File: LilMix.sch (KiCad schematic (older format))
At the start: 0 parts

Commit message: Initial version of circuit
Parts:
- added C1, C2: 10uF, symbol Device:CP
- added C? (x4): 47pF, symbol 4ms-passives:C
- added C? (x4): 100pF, symbol 4ms-passives:C
- added D1, D2: 1N5819, symbol 4ms-passives:D_Schottky
- added J1_L, J1_R, J2_L, J2_R, J3_L, J3_R, J5, J6, J? (x2): PJ301BM, Eurocad:EighthInch_PJ301BM_CC_FIXED, symbol eurocad:PJ301M-12
- added JP1: EURO_HEADER_10pin, 4ms-footprints:Header_2x05_Pitch2.54mm_TH_-12v_Label, symbol 4ms-headers:EURO_HEADER_10pin
- added R? (x8): 10k, symbol 4ms-passives:R
- added R? (x6): 100k, symbol 4ms-passives:R
- added R? (x2): 330r, symbol 4ms-passives:R
- added R? (x2): 39k, symbol 4ms-passives:R
- added R? (x2): 75r, symbol 4ms-passives:R
- added RV? (x8): A100k, symbol 4ms-mech:POT_DUAL
- added U? (x5): TL074, symbol Amplifier_Operational:TL074
- added U? (x3): NE5532, symbol Amplifier_Operational:NE5532
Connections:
- net +12V: now also C1.1, C?.1, C?.1, D1.1 (K), U?.4 (V+), U?.8 (V+)
- net -12V: now also C2.2, C?.2, C?.2, D2.2 (A), U?.11 (V-), U?.4 (V-)
- new net: D2.1 (K), JP1.10 (-12V)
- new net: D1.2 (A), JP1.2 (+12V)
- new net: C?.2, R?.1, R?.2, U?.13 (-)
- new net: C?.2, R?.1, R?.1, R?.1, R?.2, U?.2 (-)
- new net: R?.2, RV?.2 (Center) (x4)
- new net: J1_R.3, RV?.6 (Right)
- new net: J2_R.3, RV?.6 (Right)
- new net: J3_R.3, RV?.6 (Right)
- new net: C?.2, R?.1, R?.1, R?.1, R?.2, U?.6 (-)
- new net: R?.2, RV?.5 (Center) (x4)
- new net: J5.3, R?.1
- new net: J6.3, R?.1
- new net: C?.1, R?.1, R?.2, U?.8
- new net: C?.1, R?.1, R?.2, U?.14
- new net: C?.2, R?.1, R?.2, U?.9 (-)
- new net: R?.1, R?.2, U?.1
- new net: R?.1, R?.2, U?.2 (-)
- new net: R?.1, R?.2, U?.6 (-)
- new net: R?.1, R?.2, U?.7
- new net: J?.3, R?.1 (x2)
- new net GND: C1.2, C2.1, C?.1, C?.1, C?.2, C?.2, J1_L.1, J1_R.1, J2_L.1, J2_R.1, J3_L.1, J3_R.1, J5.1, J6.1, J?.1, J?.1, JP1.3 (GND), JP1.4 (GND), JP1.5 (GND), JP1.6 (GND), JP1.7 (GND), JP1.8 (GND), RV?.1 (Left), RV?.1 (Left), RV?.1 (Left), RV?.1 (Left), RV?.4 (Left), RV?.4 (Left), RV?.4 (Left), RV?.4 (Left), U?.10 (+), U?.12 (+), U?.3 (+), U?.3 (+), U?.5 (+), U?.5 (+)
- new net J1_INSERT: J1_L.3, J1_R.2, J3_R.2, RV?.3 (Right)
- new net J2_INSERT: J2_L.3, J2_R.2, RV?.3 (Right)
- new net J3_INSERT: J3_L.3, RV?.3 (Right)
- new net L_INV: C?.1, R?.1, R?.2, RV?.3 (Right), U?.1
- new net R_INV: C?.1, R?.1, R?.2, RV?.6 (Right), U?.7
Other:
- note added: "LilMix"

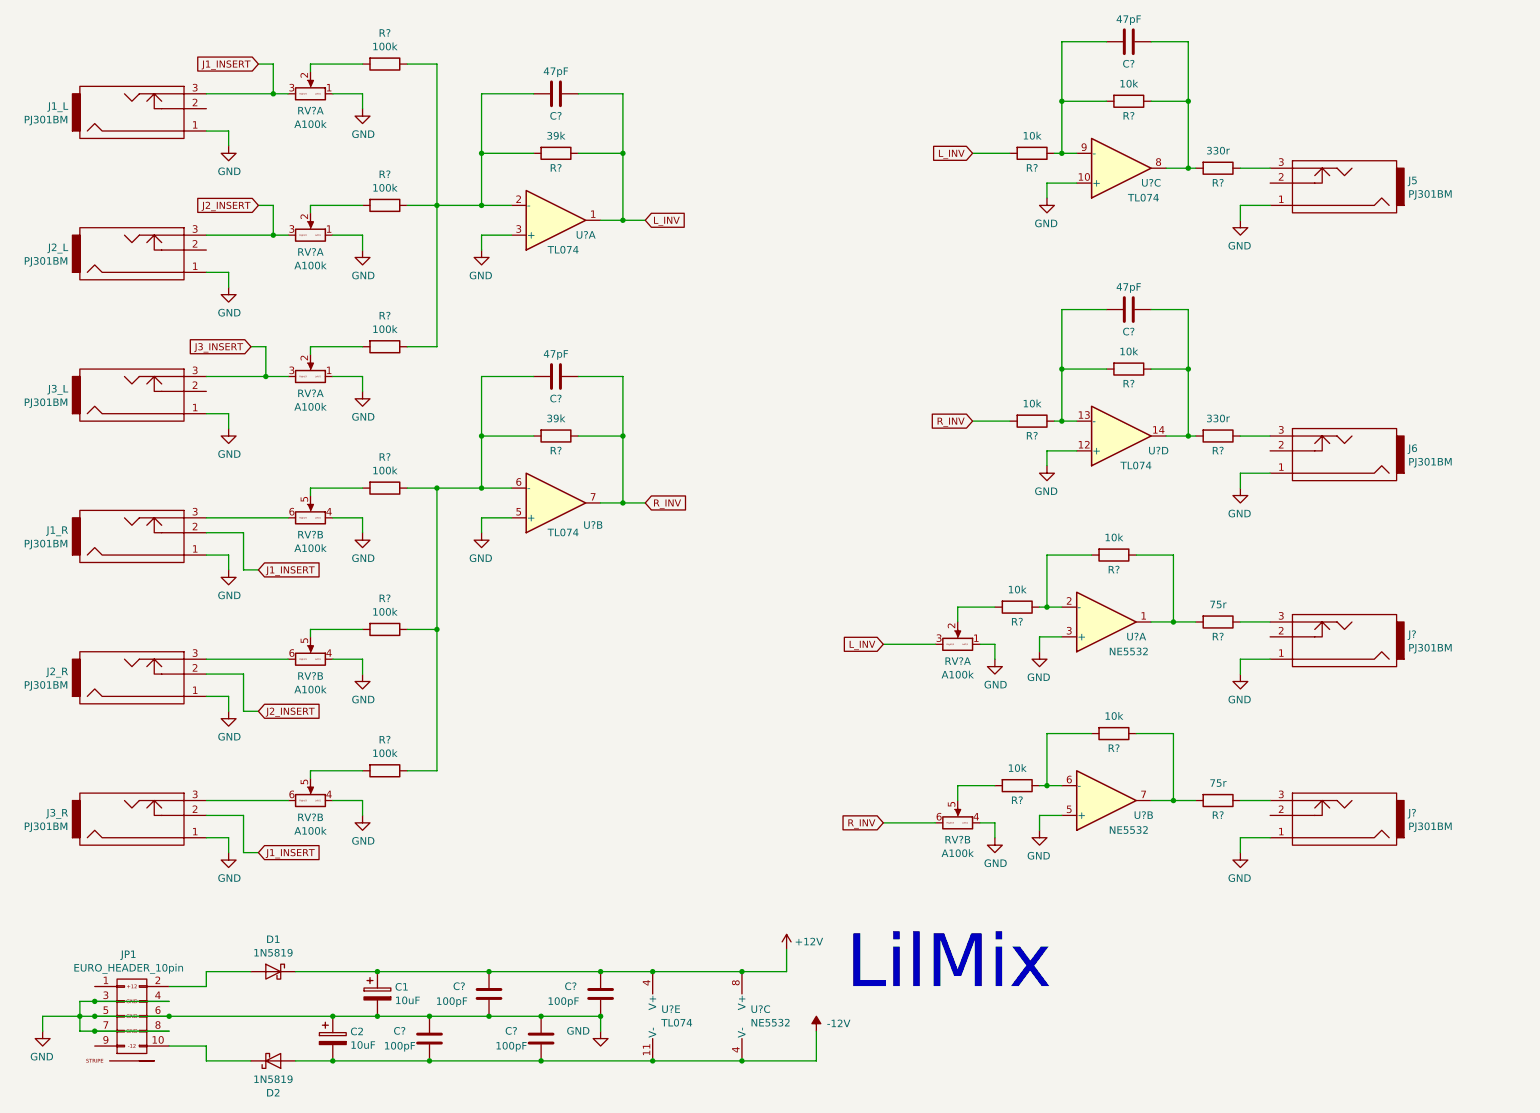
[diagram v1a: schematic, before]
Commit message: Updated to stereo jacks, replaced IC caps
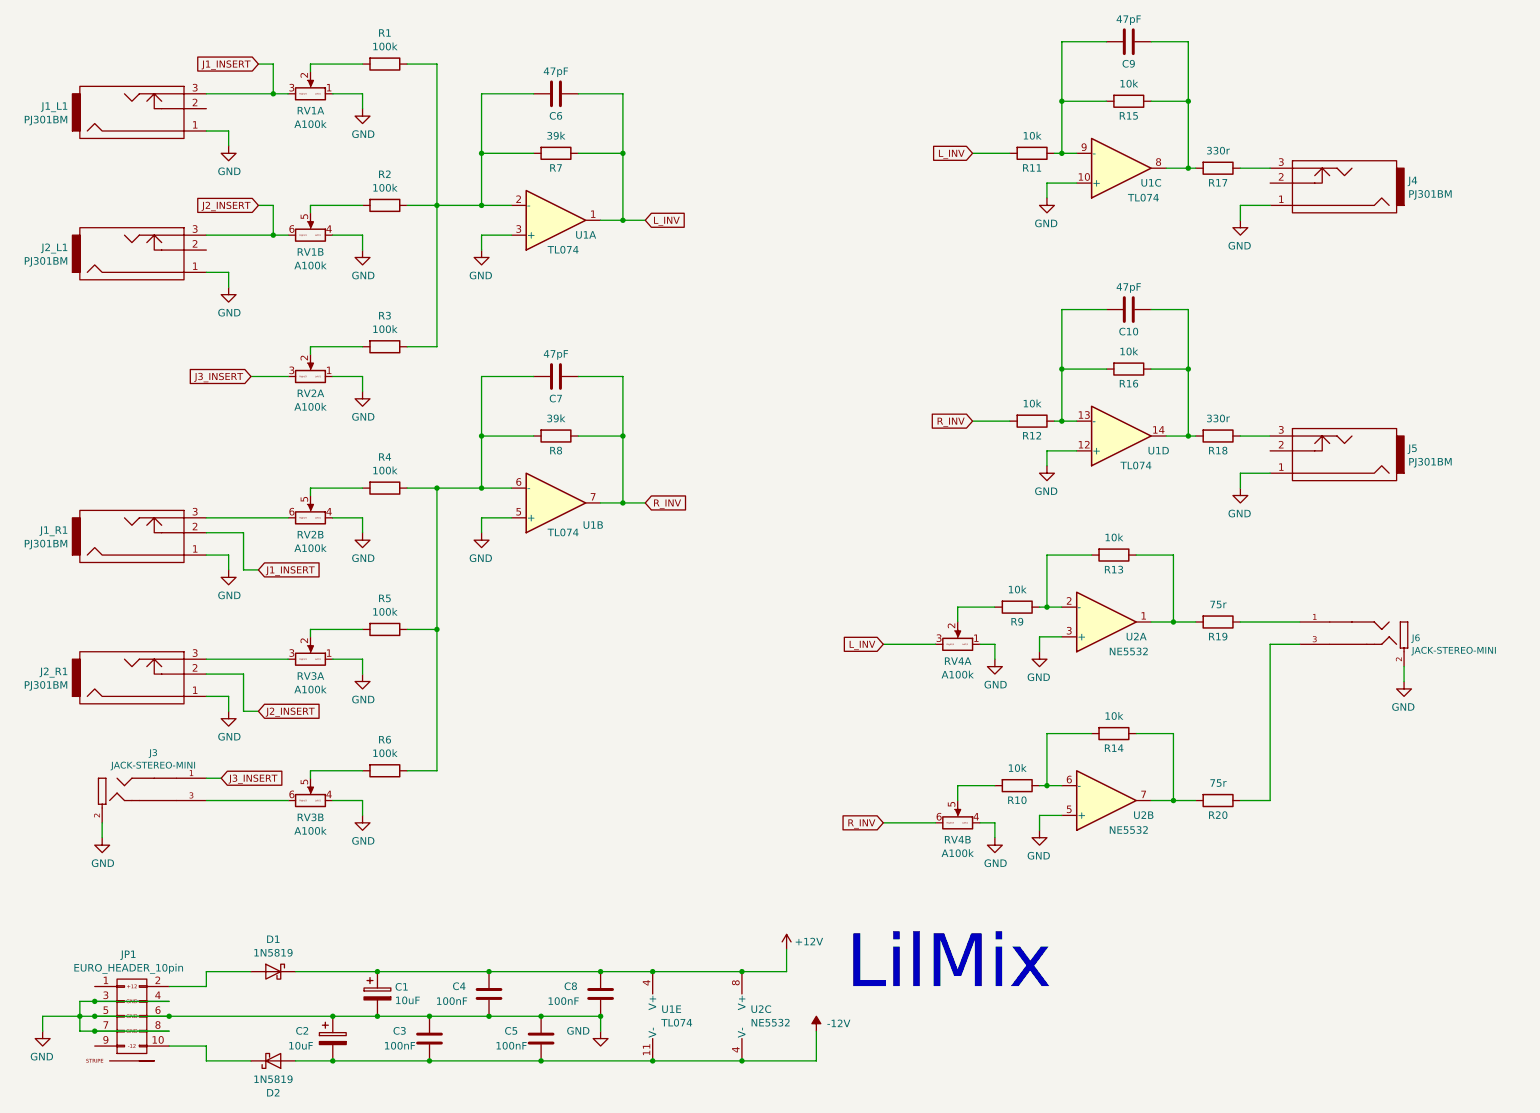
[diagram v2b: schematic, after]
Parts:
- removed J3_L, J3_R, J? (x2): PJ301BM, Eurocad:EighthInch_PJ301BM_CC_FIXED, symbol eurocad:PJ301M-12
- added J3, J6: JACK-STEREO-MINI, 4ms-footprints:PJ301M-12, symbol 4ms-mech:JACK-STEREO-MINI
- C1, C2: footprint (none) -> Capacitor_SMD:C_0805_2012Metric_Pad1.15x1.40mm_HandSolder
- C10, C6, C7, C9: renamed from C?; footprint (none) -> Capacitor_SMD:C_0805_2012Metric_Pad1.15x1.40mm_HandSolder
- C3, C4, C5, C8: renamed from C?; value 100pF -> 100nF; footprint (none) -> Capacitor_SMD:C_0805_2012Metric_Pad1.15x1.40mm_HandSolder
- D1, D2: footprint (none) -> Diode_SMD:D_SOD-123
- J1_L1: renamed from J1_L; footprint Eurocad:EighthInch_PJ301BM_CC_FIXED -> 4ms-footprints:PJ301M-12
- J1_R1: renamed from J1_R; footprint Eurocad:EighthInch_PJ301BM_CC_FIXED -> 4ms-footprints:PJ301M-12
- J2_L1: renamed from J2_L; footprint Eurocad:EighthInch_PJ301BM_CC_FIXED -> 4ms-footprints:PJ301M-12
- J2_R1: renamed from J2_R; footprint Eurocad:EighthInch_PJ301BM_CC_FIXED -> 4ms-footprints:PJ301M-12
- J4: renamed from J5; footprint Eurocad:EighthInch_PJ301BM_CC_FIXED -> 4ms-footprints:PJ301M-12
- J5: renamed from J6; footprint Eurocad:EighthInch_PJ301BM_CC_FIXED -> 4ms-footprints:PJ301M-12
- R1, R10, R11, R12, R13, R14, R15, R16, R17, R18, R19, R2, R20, R3, R4, R5, R6, R7, R8, R9: renamed from R?; footprint (none) -> Resistor_SMD:R_0805_2012Metric_Pad1.15x1.40mm_HandSolder
- RV1, RV2, RV3, RV4: renamed from RV?; footprint (none) -> Potentiometer_THT:Potentiometer_Alpha_RD902F-40-00D_Dual_Vertical
- U1: renamed from U?; footprint (none) -> Package_SO:SOIC-14_3.9x8.7mm_P1.27mm
- U2: renamed from U?; footprint (none) -> Package_SO:SOIC-8_3.9x4.9mm_P1.27mm
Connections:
- net GND: now also RV1.4 (Left), RV3.1 (Left), J3.2 (SLEEVE), J6.2 (SLEEVE); no longer RV1.1 (Left), RV3.4 (Left)
- net J2_INSERT: now also RV1.6 (Right); no longer RV1.3 (Right)
- net J3_INSERT: now also J3.1 (TIP)
- net at R2.2: now also RV1.5 (Center); no longer RV1.2 (Center)
- net at J2_R1.3: now also RV3.3 (Right); no longer RV3.6 (Right)
- net at RV3.6 (Right): now also J3.3 (TIP-SW)
- net at R5.2: now also RV3.2 (Center); no longer RV3.5 (Center)
- net at R19.1: now also J6.1 (TIP)
- net at R20.1: now also J6.3 (TIP-SW)

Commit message: Updated rough placement and circuit updates
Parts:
- added JP2, JP3: 2x4 Socket, 4ms-footprints:Socket_2x4_2.54mm_TH, symbol 4ms-headers:Conn_02x04_Odd_Even
- added RV5, RV6: 100k, 4ms-footprints:Audio_Mod_Header_1x03, symbol 4ms-mech:TRIMPOT
- JP1: value EURO_HEADER_10pin -> 2x8 Power
- R3, R6: value 100k -> 47k
- R7, R8: value 39k -> 100k
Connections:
- net labels added: GND_B, J1_L_A, J1_L_B, J1_R_A, J1_R_B, J2_L_A, J2_L_B, J2_R_A, J2_R_B, J3_L_A, J3_L_B, J3_R_A, J3_R_B
- net labels removed: J3_INSERT
- wire segments 198 -> 271
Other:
- note added: "LilMix External"
- note added: "LilMix Main"
- note removed: "LilMix"
- moved on the sheet: C1, C10, C2, C3, C4, C5, C6, C7, C8, C9, D1, D2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

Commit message: Rought placement complete
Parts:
- J1_L1, J1_R1, J2_L1, J2_R1, J4, J5: value PJ301BM -> MONO
- J3, J6: value JACK-STEREO-MINI -> STEREO
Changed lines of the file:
@@
 P -6850 2450
 F 0 "J3" H -6905 2720 45  0000 C CNN
-F 1 "JACK-STEREO-MINI" H -6905 2636 45  0000 C CNN
+F 1 "STEREO" H -6905 2636 45  0000 C CNN
 F 2 "4ms-footprints:PJ301M-12" H -6820 2600 20  0001 C CNN
 F 3 "" H -6850 2450 60  0001 C CNN
@@
 P 9050 4700
 F 0 "J6" H 8598 4692 45  0000 R CNN
-F 1 "JACK-STEREO-MINI" H 8598 4608 45  0000 R CNN
+F 1 "STEREO" H 8598 4608 45  0000 R CNN
 F 2 "4ms-footprints:PJ301M-12" H 9080 4850 20  0001 C CNN
 F 3 "" H 9050 4700 60  0001 C CNN
@@
 P 8950 3300
 F 0 "J5" H 8472 3284 50  0000 R CNN
-F 1 "PJ301BM" H 8472 3375 50  0000 R CNN
+F 1 "MONO" H 8472 3375 50  0000 R CNN
 F 2 "4ms-footprints:PJ301M-12" H 8950 3300 50  0001 C CNN
 F 3 "" H 8950 3300 50  0000 C CNN
@@
 P 8950 1700
 F 0 "J4" H 8472 1684 50  0000 R CNN
-F 1 "PJ301BM" H 8472 1775 50  0000 R CNN
+F 1 "MONO" H 8472 1775 50  0000 R CNN
 F 2 "4ms-footprints:PJ301M-12" H 8950 1700 50  0001 C CNN
 F 3 "" H 8950 1700 50  0000 C CNN
@@
 P -5650 5950
 F 0 "J2_R1" H -6128 5934 50  0000 R CNN
-F 1 "PJ301BM" H -6128 6025 50  0000 R CNN
+F 1 "MONO" H -6128 6025 50  0000 R CNN
 F 2 "4ms-footprints:PJ301M-12" H -5650 5950 50  0001 C CNN
 F 3 "" H -5650 5950 50  0000 C CNN
@@
 P -6300 5050
 F 0 "J1_R1" H -6778 5034 50  0000 R CNN
-F 1 "PJ301BM" H -6778 5125 50  0000 R CNN
+F 1 "MONO" H -6778 5125 50  0000 R CNN
 F 2 "4ms-footprints:PJ301M-12" H -6300 5050 50  0001 C CNN
 F 3 "" H -6300 5050 50  0000 C CNN
@@
 P -7500 3450
 F 0 "J1_L1" H -7978 3434 50  0000 R CNN
-F 1 "PJ301BM" H -7978 3525 50  0000 R CNN
+F 1 "MONO" H -7978 3525 50  0000 R CNN
 F 2 "4ms-footprints:PJ301M-12" H -7500 3450 50  0001 C CNN
 F 3 "" H -7500 3450 50  0000 C CNN
@@
 P -6850 4250
 F 0 "J2_L1" H -7328 4234 50  0000 R CNN
-F 1 "PJ301BM" H -7328 4325 50  0000 R CNN
+F 1 "MONO" H -7328 4325 50  0000 R CNN
 F 2 "4ms-footprints:PJ301M-12" H -6850 4250 50  0001 C CNN
 F 3 "" H -6850 4250 50  0000 C CNN

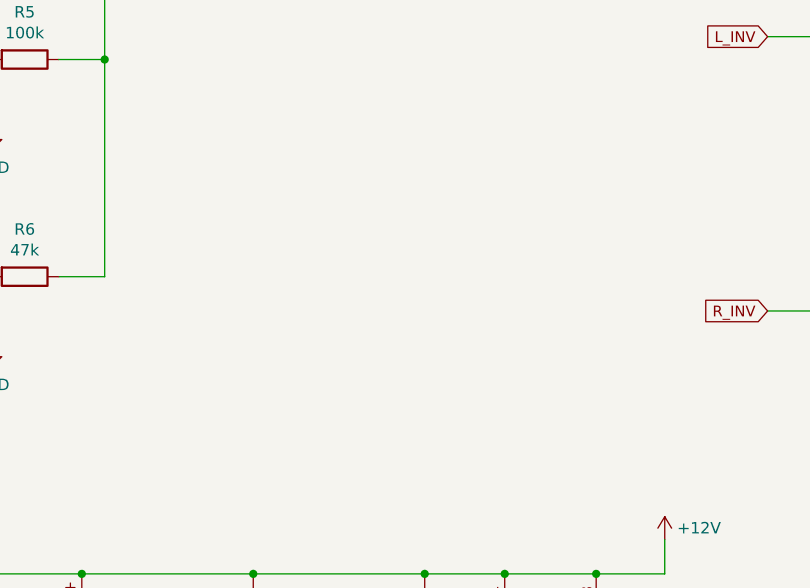
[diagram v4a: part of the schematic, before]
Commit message: Added power sockets for other modules
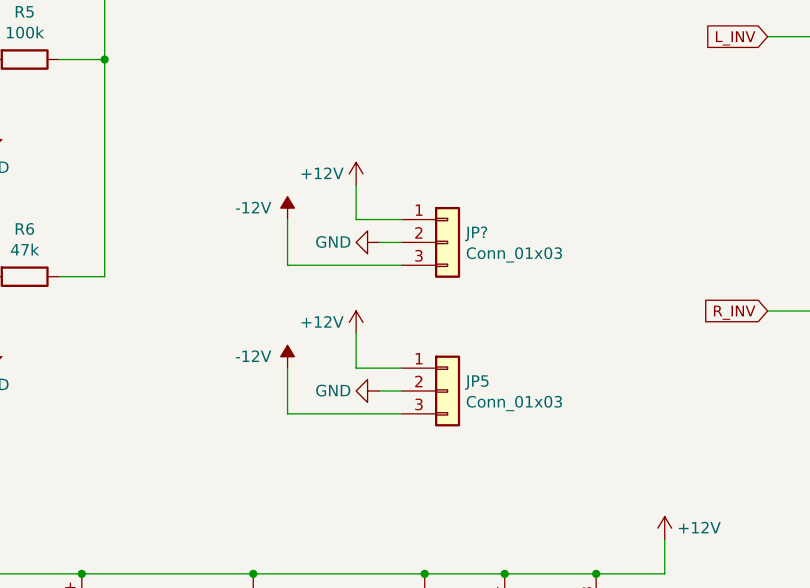
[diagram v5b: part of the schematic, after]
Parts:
- added JP5, JP?: Conn_01x03, Connector_PinSocket_2.54mm:PinSocket_1x03_P2.54mm_Vertical, symbol 4ms-headers:Conn_01x03
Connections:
- wire segments 271 -> 281
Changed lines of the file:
@@
 Wire Wire Line
 	1800 7600 1900 7600
+Wire Wire Line
+	4350 6400 3850 6400
+Wire Wire Line
+	4150 6200 4350 6200
+Wire Wire Line
+	3850 6400 3850 6200
+$Comp
+L power:-12V #PWR0106
+U 1 1 5E5ADB7B
+P 3850 6200
+F 0 "#PWR0106" H 3850 6300 50  0001 C CNN
+F 1 "-12V" H 4000 6250 50  0000 C CNN
+F 2 "" H 3850 6200 50  0001 C CNN
+F 3 "" H 3850 6200 50  0001 C CNN
+	1    3850 6200
+	-1   0    0    -1
+$EndComp
+Wire Wire Line
+	4150 6200 4150 6050
+$Comp
+L power:+12V #PWR0108
+U 1 1 5E5ADB86
+P 4150 6050
+F 0 "#PWR0108" H 4150 5900 50  0001 C CNN
+F 1 "+12V" H 4300 6100 50  0000 C CNN
+F 2 "" H 4150 6050 50  0001 C CNN
+F 3 "" H 4150 6050 50  0001 C CNN
+	1    4150 6050
+	-1   0    0    -1
+$EndComp
+$Comp
+L 4ms-headers:Conn_01x03 JP5
+U 1 1 5E5D141C
+P 4550 6300
+F 0 "JP5" H 4630 6342 50  0000 L CNN
+F 1 "Conn_01x03" H 4630 6251 50  0000 L CNN
+F 2 "Connector_PinSocket_2.54mm:PinSocket_1x03_P2.54mm_Vertical" H 4550 6300 50  0001 C CNN
+F 3 "" H 4550 6300 50  0001 C CNN
+	1    4550 6300
+	1    0    0    -1
+$EndComp
+$Comp
+L 4ms-power:GND #PWR0110
+U 1 1 5E64C05E
+P 4250 6300
+F 0 "#PWR0110" H 4250 6050 50  0001 C CNN
+F 1 "GND" V 4250 6100 50  0000 C CNN
+F 2 "" H 4250 6300 50  0001 C CNN
+F 3 "" H 4250 6300 50  0001 C CNN
+	1    4250 6300
+	0    1    1    0
+$EndComp
+Wire Wire Line
+	4350 6300 4250 6300
+Wire Wire Line
+	4350 5750 3850 5750
+Wire Wire Line
+	4150 5550 4350 5550
+Wire Wire Line
+	3850 5750 3850 5550
+$Comp
+L power:-12V #PWR?
+U 1 1 5E69B760
+P 3850 5550
+F 0 "#PWR?" H 3850 5650 50  0001 C CNN
+F 1 "-12V" H 4000 5600 50  0000 C CNN
+F 2 "" H 3850 5550 50  0001 C CNN
+F 3 "" H 3850 5550 50  0001 C CNN
+	1    3850 5550
+	-1   0    0    -1
+$EndComp
+Wire Wire Line
+	4150 5550 4150 5400
+$Comp
+L power:+12V #PWR?
+U 1 1 5E69B76B
+P 4150 5400
+F 0 "#PWR?" H 4150 5250 50  0001 C CNN
+F 1 "+12V" H 4300 5450 50  0000 C CNN
+F 2 "" H 4150 5400 50  0001 C CNN
+F 3 "" H 4150 5400 50  0001 C CNN
+	1    4150 5400
+	-1   0    0    -1
+$EndComp
+$Comp
+L 4ms-headers:Conn_01x03 JP?
+U 1 1 5E69B775
+P 4550 5650
+F 0 "JP?" H 4630 5692 50  0000 L CNN
+F 1 "Conn_01x03" H 4630 5601 50  0000 L CNN
+F 2 "Connector_PinSocket_2.54mm:PinSocket_1x03_P2.54mm_Vertical" H 4550 5650 50  0001 C CNN
+F 3 "" H 4550 5650 50  0001 C CNN
+	1    4550 5650
+	1    0    0    -1
+$EndComp
+$Comp
+L 4ms-power:GND #PWR?
+U 1 1 5E69B77F
+P 4250 5650
+F 0 "#PWR?" H 4250 5400 50  0001 C CNN
+F 1 "GND" V 4250 5450 50  0000 C CNN
+F 2 "" H 4250 5650 50  0001 C CNN
+F 3 "" H 4250 5650 50  0001 C CNN
+	1    4250 5650
+	0    1    1    0
+$EndComp
+Wire Wire Line
+	4350 5650 4250 5650
 $EndSCHEMATC

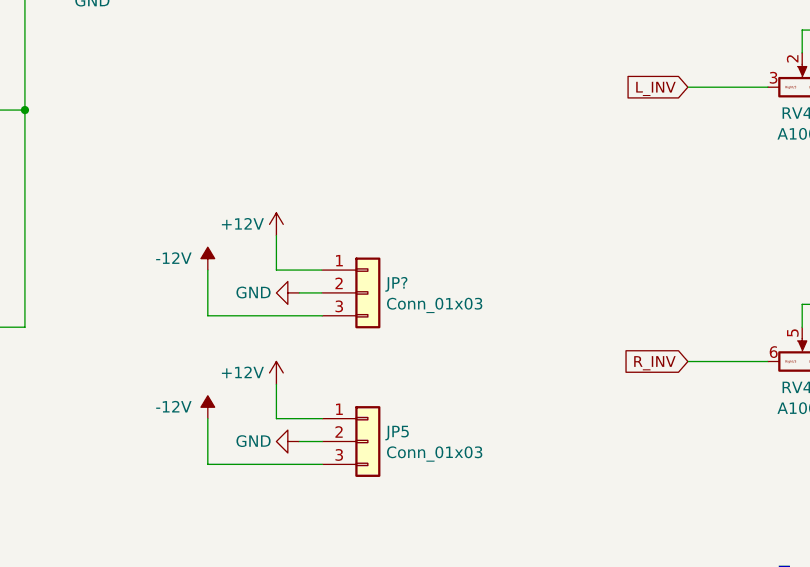
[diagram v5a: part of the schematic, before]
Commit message: Updated footprint of stereo jacks
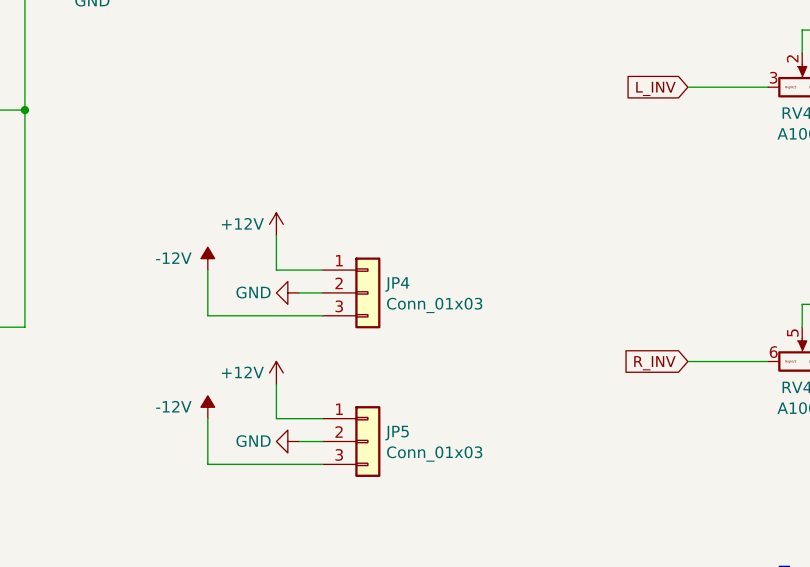
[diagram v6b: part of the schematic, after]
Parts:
- J3, J6: footprint 4ms-footprints:PJ301M-12 -> Eurocad:STPX-3501-3C-1
- gave numbers to parts that had none: 1
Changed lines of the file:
@@
 F 0 "J3" H -6905 2720 45  0000 C CNN
 F 1 "STEREO" H -6905 2636 45  0000 C CNN
-F 2 "4ms-footprints:PJ301M-12" H -6820 2600 20  0001 C CNN
+F 2 "Eurocad:STPX-3501-3C-1" H -6820 2600 20  0001 C CNN
 F 3 "" H -6850 2450 60  0001 C CNN
 	1    -6850 2450
@@
 F 0 "J6" H 8598 4692 45  0000 R CNN
 F 1 "STEREO" H 8598 4608 45  0000 R CNN
-F 2 "4ms-footprints:PJ301M-12" H 9080 4850 20  0001 C CNN
+F 2 "Eurocad:STPX-3501-3C-1" H 9080 4850 20  0001 C CNN
 F 3 "" H 9050 4700 60  0001 C CNN
 	1    9050 4700
@@
 	3850 5750 3850 5550
 $Comp
-L power:-12V #PWR?
+L power:-12V #PWR0129
 U 1 1 5E69B760
 P 3850 5550
-F 0 "#PWR?" H 3850 5650 50  0001 C CNN
+F 0 "#PWR0129" H 3850 5650 50  0001 C CNN
 F 1 "-12V" H 4000 5600 50  0000 C CNN
 F 2 "" H 3850 5550 50  0001 C CNN
@@
 	4150 5550 4150 5400
 $Comp
-L power:+12V #PWR?
+L power:+12V #PWR0130
 U 1 1 5E69B76B
 P 4150 5400
-F 0 "#PWR?" H 4150 5250 50  0001 C CNN
+F 0 "#PWR0130" H 4150 5250 50  0001 C CNN
 F 1 "+12V" H 4300 5450 50  0000 C CNN
 F 2 "" H 4150 5400 50  0001 C CNN
@@
 $EndComp
 $Comp
-L 4ms-headers:Conn_01x03 JP?
+L 4ms-headers:Conn_01x03 JP4
 U 1 1 5E69B775
 P 4550 5650
-F 0 "JP?" H 4630 5692 50  0000 L CNN
+F 0 "JP4" H 4630 5692 50  0000 L CNN
 F 1 "Conn_01x03" H 4630 5601 50  0000 L CNN
 F 2 "Connector_PinSocket_2.54mm:PinSocket_1x03_P2.54mm_Vertical" H 4550 5650 50  0001 C CNN
@@
 $EndComp
 $Comp
-L 4ms-power:GND #PWR?
+L 4ms-power:GND #PWR0131
 U 1 1 5E69B77F
 P 4250 5650
-F 0 "#PWR?" H 4250 5400 50  0001 C CNN
+F 0 "#PWR0131" H 4250 5400 50  0001 C CNN
 F 1 "GND" V 4250 5450 50  0000 C CNN
 F 2 "" H 4250 5650 50  0001 C CNN
